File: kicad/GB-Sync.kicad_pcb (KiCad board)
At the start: 2 copper layers, 18.1 x 18.1 mm, 5 parts

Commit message: Added repo url on back silkscreen and minor text changes
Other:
- board text added: "git.io/fAoFv"
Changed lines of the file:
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@@
   (general
     (thickness 1.6)
-    (drawings 17)
+    (drawings 18)
     (tracks 70)
     (zones 0)
@@
     (34 B.Paste user)
     (35 F.Paste user)
-    (36 B.SilkS user hide)
+    (36 B.SilkS user)
     (37 F.SilkS user)
     (38 B.Mask user)
@@
       (net 11 "Net-(conn5-Pad1)"))
   )
+  (gr_text "   git.io/fAoFv" (at 152.4 101.6) (layer B.SilkS)
+    (effects (font (size 0.4 0.4) (thickness 0.075)) (justify mirror))
+  )
   (gr_text "For MGB/CGB link" (at 154.94 101.6) (layer F.SilkS)
     (effects (font (size 0.3 0.3) (thickness 0.075)) (justify right))
@@
   )
   (gr_text "Lesbinary\n2018/09" (at 149.86 97.79) (layer B.SilkS)
-    (effects (font (size 0.7 0.7) (thickness 0.175)) (justify right mirror))
+    (effects (font (size 0.5 0.5) (thickness 0.125)) (justify right mirror))
   )
   (gr_text ". ." (at 151.6888 89.7636) (layer F.SilkS)

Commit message: Changed link
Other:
- board text added: "git.io/fAiCn"
- board text removed: "git.io/fAoFv"
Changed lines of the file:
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@@
       (net 11 "Net-(conn5-Pad1)"))
   )
-  (gr_text "   git.io/fAoFv" (at 152.4 101.6) (layer B.SilkS)
+  (gr_text "   git.io/fAiCn" (at 152.4 101.6) (layer B.SilkS)
     (effects (font (size 0.4 0.4) (thickness 0.075)) (justify mirror))
   )

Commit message: Changed PCB info
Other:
- board text added: "Poldet 18/10"
- board text added: "git.io/fxJFF"
- board text removed: "Lesbinary 2018/09"
- board text removed: "git.io/fAiCn"
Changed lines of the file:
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@@
       (net 11 "Net-(conn5-Pad1)"))
   )
-  (gr_text "   git.io/fAiCn" (at 152.4 101.6) (layer B.SilkS)
+  (gr_text "   git.io/fxJFF" (at 152.4 101.6) (layer B.SilkS)
     (effects (font (size 0.4 0.4) (thickness 0.075)) (justify mirror))
   )
@@
     (effects (font (size 0.5 0.5) (thickness 0.125)) (justify right))
   )
-  (gr_text "Lesbinary\n2018/09" (at 149.86 97.79) (layer B.SilkS)
+  (gr_text "Poldet  \n18/10  " (at 149.86 97.79) (layer B.SilkS)
     (effects (font (size 0.5 0.5) (thickness 0.125)) (justify right mirror))
   )

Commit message: Deleted some info
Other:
- board text added: "2018/10"
- board text removed: "Poldet 18/10"
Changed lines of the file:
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@@
     (effects (font (size 0.5 0.5) (thickness 0.125)) (justify right))
   )
-  (gr_text "Poldet  \n18/10  " (at 149.86 97.79) (layer B.SilkS)
+  (gr_text "\n2018/10" (at 149.86 97.79) (layer B.SilkS)
     (effects (font (size 0.5 0.5) (thickness 0.125)) (justify right mirror))
   )

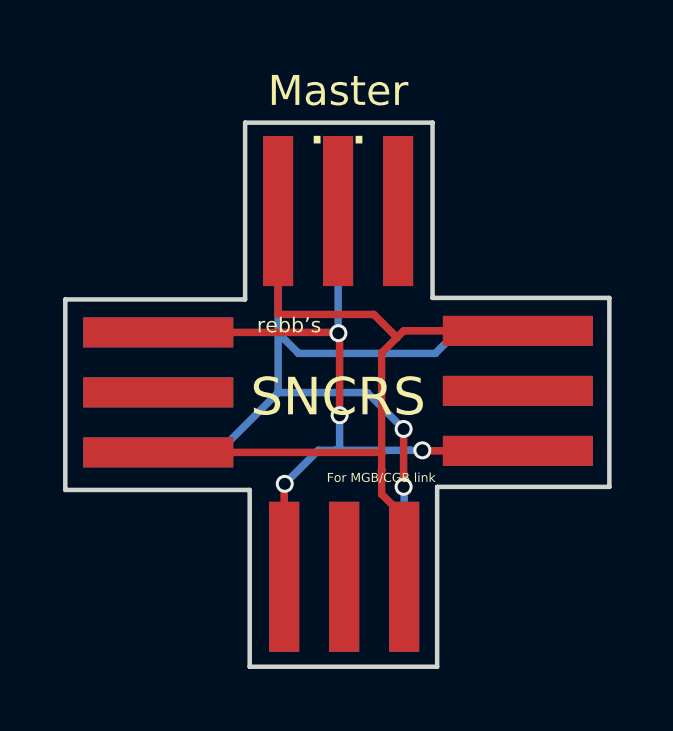
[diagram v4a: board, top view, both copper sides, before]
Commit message: Refactored with real Link Port measurements
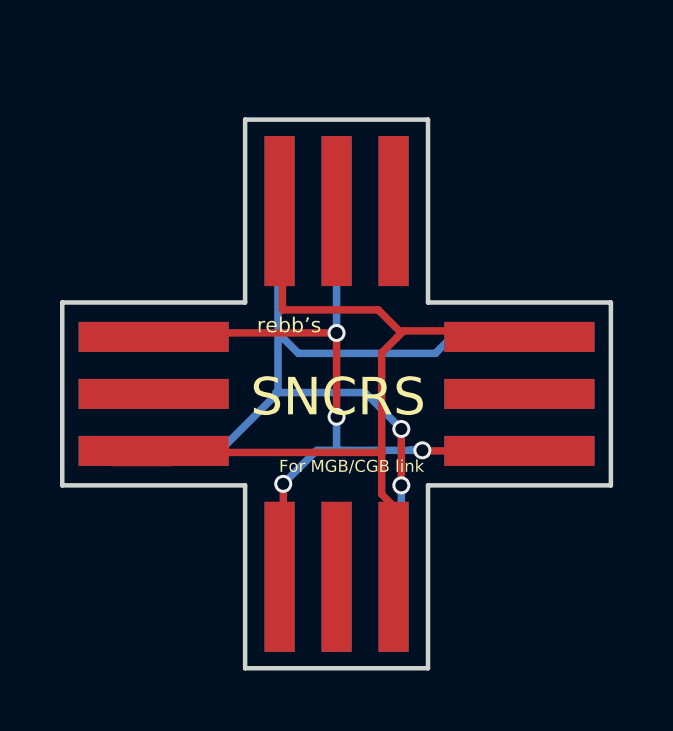
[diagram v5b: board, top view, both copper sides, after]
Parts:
- G***: value tplogo -> LOGO
- moved G*** 1.33 mm to (150.2, 99.1)
- moved ? 0.25 mm to (151.6, 104.9)
- moved ? 0.16 mm to (145.5, 98.8)
- moved ? 0.11 mm to (157.7, 98.8)
- moved Master 0.05 mm to (151.6, 92.7)
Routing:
- net Net-(conn1-Pad3): track 37.4 -> 38.0 mm
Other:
- board size 18.1 x 18.1 mm -> 18.3 x 18.3 mm
- board text added: "Poldet"
- board text removed: ". ."
